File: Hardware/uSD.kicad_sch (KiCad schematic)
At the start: 2 parts, among them J12 MSD-4-A

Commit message: S31 fully connected
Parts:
- added D10, D11, D12, D2, D4, D5, D9: BSDFN2C031U, PCM_JLCPCB:D_DFN1006-2L, symbol YV-library:TVS-BSDFN2C031U
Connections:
- net +3.3V: now also D12.2 (A2)
- net CLK: now also D5.2 (A2)
- net CMD: now also D9.2 (A2)
- net DATA0: now also D4.2 (A2)
- net DATA1: now also D2.2 (A2)
- net DATA2: now also D11.2 (A2)
- net DATA3: now also D10.2 (A2)
- net GND: now also D10.1 (A1), D11.1 (A1), D12.1 (A1), D2.1 (A1), D4.1 (A1), D5.1 (A1), D9.1 (A1)
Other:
- moved on the sheet: C28

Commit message: Schematic Done
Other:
- company: (none) -> Motion Composites
- title: (none) -> Strain Gauge Data Logger
- moved on the sheet: D10, D11, D12, D2, D4, D5, D9

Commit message: Layout cleaned
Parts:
- renumbered C28 to C1, D11 to D1, D10 to D2, D9 to D3, D12 to D4, D4 to D6, D2 to D8, J12 to J4
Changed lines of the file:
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@@
 		(in_pos_files yes)
 		(dnp no)
-		(property "Reference" "D10"
+		(property "Reference" "D2"
 			(at 114.3 116.332 0)
 			(show_name no)
@@
 			(project "esp32-V2"
 				(path "/cee18f8d-8618-44b5-96f4-3f3967d85a92/90fb081b-c808-4d88-91aa-e417d2abcc14"
-					(reference "D10")
+					(reference "D2")
 					(unit 1)
 				)
@@
 		(in_pos_files yes)
 		(dnp no)
-		(property "Reference" "D11"
+		(property "Reference" "D1"
 			(at 118.11 116.332 0)
 			(show_name no)
@@
 			(project "esp32-V2"
 				(path "/cee18f8d-8618-44b5-96f4-3f3967d85a92/90fb081b-c808-4d88-91aa-e417d2abcc14"
-					(reference "D11")
+					(reference "D1")
 					(unit 1)
 				)
@@
 		(in_pos_files yes)
 		(dnp no)
-		(property "Reference" "D9"
+		(property "Reference" "D3"
 			(at 110.49 117.602 0)
 			(show_name no)
@@
 			(project "esp32-V2"
 				(path "/cee18f8d-8618-44b5-96f4-3f3967d85a92/90fb081b-c808-4d88-91aa-e417d2abcc14"
-					(reference "D9")
+					(reference "D3")
 					(unit 1)
 				)
@@
 		(dnp no)
 		(fields_autoplaced yes)
-		(property "Reference" "J12"
+		(property "Reference" "J4"
 			(at 180.34 101.5999 0)
 			(show_name no)
@@
 			(project "esp32-V2"
 				(path "/cee18f8d-8618-44b5-96f4-3f3967d85a92/90fb081b-c808-4d88-91aa-e417d2abcc14"
-					(reference "J12")
+					(reference "J4")
 					(unit 1)
 				)
@@
 		(in_pos_files yes)
 		(dnp no)
-		(property "Reference" "D4"
+		(property "Reference" "D6"
 			(at 102.87 117.602 0)
 			(show_name no)
@@
 			(project "esp32-V2"
 				(path "/cee18f8d-8618-44b5-96f4-3f3967d85a92/90fb081b-c808-4d88-91aa-e417d2abcc14"
-					(reference "D4")
+					(reference "D6")
 					(unit 1)
 				)
@@
 		(in_pos_files yes)
 		(dnp no)
-		(property "Reference" "C28"
+		(property "Reference" "C1"
 			(at 129.794 80.264 0)
 			(show_name no)
@@
 			(project "esp32-V2"
 				(path "/cee18f8d-8618-44b5-96f4-3f3967d85a92/90fb081b-c808-4d88-91aa-e417d2abcc14"
-					(reference "C28")
+					(reference "C1")
 					(unit 1)
 				)
@@
 		(in_pos_files yes)
 		(dnp no)
-		(property "Reference" "D12"
+		(property "Reference" "D4"
 			(at 121.92 116.332 0)
 			(show_name no)
@@
 			(project "esp32-V2"
 				(path "/cee18f8d-8618-44b5-96f4-3f3967d85a92/90fb081b-c808-4d88-91aa-e417d2abcc14"
-					(reference "D12")
+					(reference "D4")
 					(unit 1)
 				)
@@
 		(in_pos_files yes)
 		(dnp no)
-		(property "Reference" "D2"
+		(property "Reference" "D8"
 			(at 98.806 117.602 0)
 			(show_name no)
@@
 			(project "esp32-V2"
 				(path "/cee18f8d-8618-44b5-96f4-3f3967d85a92/90fb081b-c808-4d88-91aa-e417d2abcc14"
-					(reference "D2")
+					(reference "D8")
 					(unit 1)
 				)

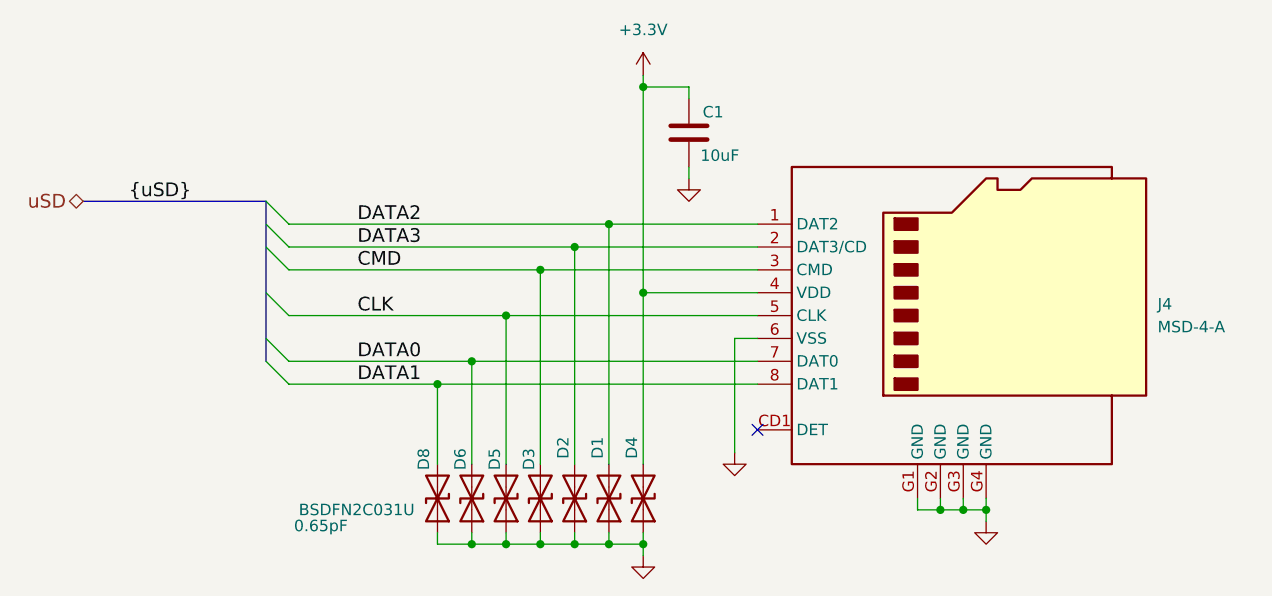
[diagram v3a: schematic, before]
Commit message: Update de la librairy et du BOM
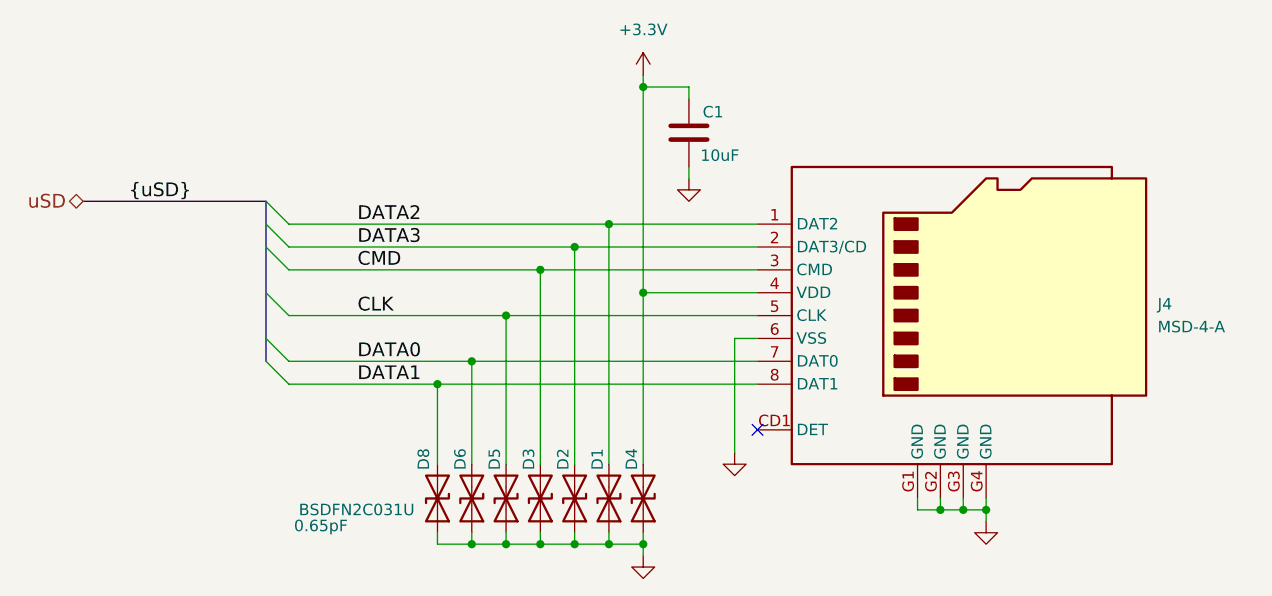
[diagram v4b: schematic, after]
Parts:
- C1: symbol Device:C -> YV-library:CAPX10U0M6V30-00; KiLib_Generator SMD_2terminal_chip_molded -> (none); LCSC C20069813 -> C15525; PartNumber (none) -> CL05A106MQ5NUNC
- D1, D2, D3, D4, D5, D6: Capacitance (none) -> 0.65pF
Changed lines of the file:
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@@
 		(dnp no)
 		(property "Reference" "D2"
-			(at 114.3 116.332 0)
+			(at 114.3 117.602 0)
 			(show_name no)
 			(do_not_autoplace no)
@@
 			)
 		)
-		(property "Description" "0.65pF 3.3V 500nA 50W@8/20us TVS, 6.2V, 7A@8/20us, Bidirectional, IEC 61000-4-2、IEC 61000-4-5、IEC 61000-4-4 DFN1006-2"
+		(property "Description" "TVS, 0.65pF, 3.3V, 500nA, 50W@8/20us, 6.2V, 7A@8/20us, Bidirectional"
 			(at 115.57 123.19 0)
 			(hide yes)
@@
 		(property "LCSC" "C600818"
 			(at 115.57 123.19 0)
+			(hide yes)
+			(show_name no)
+			(do_not_autoplace no)
+			(effects
+				(font
+					(size 1.27 1.27)
+				)
+			)
+		)
+		(property "Capacitance" "0.65pF"
+			(at 112.522 123.19 0)
 			(hide yes)
 			(show_name no)
@@
 		(dnp no)
 		(property "Reference" "D1"
-			(at 118.11 116.332 0)
+			(at 118.11 117.602 0)
 			(show_name no)
 			(do_not_autoplace no)
@@
 			)
 		)
-		(property "Description" "0.65pF 3.3V 500nA 50W@8/20us TVS, 6.2V, 7A@8/20us, Bidirectional, IEC 61000-4-2、IEC 61000-4-5、IEC 61000-4-4 DFN1006-2"
+		(property "Description" "TVS, 0.65pF, 3.3V, 500nA, 50W@8/20us, 6.2V, 7A@8/20us, Bidirectional"
 			(at 119.38 123.19 0)
 			(hide yes)
@@
 		(property "LCSC" "C600818"
 			(at 119.38 123.19 0)
+			(hide yes)
+			(show_name no)
+			(do_not_autoplace no)
+			(effects
+				(font
+					(size 1.27 1.27)
+				)
+			)
+		)
+		(property "Capacitance" "0.65pF"
+			(at 116.332 123.19 0)
 			(hide yes)
 			(show_name no)
@@
 			)
 		)
-		(property "Description" "0.65pF 3.3V 500nA 50W@8/20us TVS, 6.2V, 7A@8/20us, Bidirectional, IEC 61000-4-2、IEC 61000-4-5、IEC 61000-4-4 DFN1006-2"
+		(property "Description" "TVS, 0.65pF, 3.3V, 500nA, 50W@8/20us, 6.2V, 7A@8/20us, Bidirectional"
 			(at 111.76 123.19 0)
 			(hide yes)
@@
 		(property "LCSC" "C600818"
 			(at 111.76 123.19 0)
+			(hide yes)
+			(show_name no)
+			(do_not_autoplace no)
+			(effects
+				(font
+					(size 1.27 1.27)
+				)
+			)
+		)
+		(property "Capacitance" "0.65pF"
+			(at 108.712 123.19 0)
 			(hide yes)
 			(show_name no)
@@
 			)
 		)
-		(property "Description" "Micro SD Card Socket with one card detection pin"
+		(property "Description" "Connector, Micro SD Card Socket with one card detection pin"
 			(at 158.75 102.87 0)
 			(hide yes)
@@
 			)
 		)
-		(property "Description" "0.65pF 3.3V 500nA 50W@8/20us TVS, 6.2V, 7A@8/20us, Bidirectional, IEC 61000-4-2、IEC 61000-4-5、IEC 61000-4-4 DFN1006-2"
+		(property "Description" "TVS, 0.65pF, 3.3V, 500nA, 50W@8/20us, 6.2V, 7A@8/20us, Bidirectional"
 			(at 104.14 123.19 0)
 			(hide yes)
@@
 		(property "LCSC" "C600818"
 			(at 104.14 123.19 0)
+			(hide yes)
+			(show_name no)
+			(do_not_autoplace no)
+			(effects
+				(font
+					(size 1.27 1.27)
+				)
+			)
+		)
+		(property "Capacitance" "0.65pF"
+			(at 101.092 123.19 0)
 			(hide yes)
 			(show_name no)
@@
 			)
 		)
-		(property "Description" "0.65pF 3.3V 500nA 50W@8/20us TVS, 6.2V, 7A@8/20us, Bidirectional, IEC 61000-4-2、IEC 61000-4-5、IEC 61000-4-4 DFN1006-2"
+		(property "Description" "TVS, 0.65pF, 3.3V, 500nA, 50W@8/20us, 6.2V, 7A@8/20us, Bidirectional"
 			(at 107.95 123.19 0)
 			(hide yes)
@@
 		(property "LCSC" "C600818"
 			(at 107.95 123.19 0)
+			(hide yes)
+			(show_name no)
+			(do_not_autoplace no)
+			(effects
+				(font
+					(size 1.27 1.27)
+				)
+			)
+		)
+		(property "Capacitance" "0.65pF"
+			(at 104.902 123.19 0)
 			(hide yes)
 			(show_name no)
@@
 	)
 	(symbol
-		(lib_id "Device:C")
+		(lib_id "YV-library:CAPX10U0M6V30-00")
 		(at 128.27 82.55 0)
 		(unit 1)
@@
 			)
 		)
-		(property "Description" "Unpolarized capacitor"
+		(property "Description" "Cap X5R, 10uF, 6.3V, ±20%, 0402"
 			(at 128.27 82.55 0)
 			(hide yes)
@@
 			)
 		)
-		(property "KiLib_Generator" "SMD_2terminal_chip_molded"
+		(property "LCSC" "C15525"
 			(at 128.27 82.55 0)
 			(hide yes)
@@
 			)
 		)
-		(property "LCSC" "C20069813"
+		(property "PartNumber" "CL05A106MQ5NUNC"
 			(at 128.27 82.55 0)
 			(hide yes)
@@
 		(dnp no)
 		(property "Reference" "D4"
-			(at 121.92 116.332 0)
+			(at 121.92 117.602 0)
 			(show_name no)
 			(do_not_autoplace no)
@@
 			)
 		)
-		(property "Description" "0.65pF 3.3V 500nA 50W@8/20us TVS, 6.2V, 7A@8/20us, Bidirectional, IEC 61000-4-2、IEC 61000-4-5、IEC 61000-4-4 DFN1006-2"
+		(property "Description" "TVS, 0.65pF, 3.3V, 500nA, 50W@8/20us, 6.2V, 7A@8/20us, Bidirectional"
 			(at 123.19 123.19 0)
 			(hide yes)
@@
 		(property "LCSC" "C600818"
 			(at 123.19 123.19 0)
+			(hide yes)
+			(show_name no)
+			(do_not_autoplace no)
+			(effects
+				(font
+					(size 1.27 1.27)
+				)
+			)
+		)
+		(property "Capacitance" "0.65pF"
+			(at 120.142 123.19 0)
 			(hide yes)
 			(show_name no)
@@
 			)
 		)
-		(property "Description" "0.65pF 3.3V 500nA 50W@8/20us TVS, 6.2V, 7A@8/20us, Bidirectional, IEC 61000-4-2、IEC 61000-4-5、IEC 61000-4-4 DFN1006-2"
+		(property "Description" "TVS, 0.65pF, 3.3V, 500nA, 50W@8/20us, 6.2V, 7A@8/20us, Bidirectional"
 			(at 100.33 123.19 0)
 			(hide yes)
